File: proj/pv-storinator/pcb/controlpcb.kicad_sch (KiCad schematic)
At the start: 65 parts, among them J1 Conn_01x06_Socket, J10 Conn_01x01, J11 Conn_01x01, J12 Conn_01x06_Socket, J13 Conn_01x07_Socket, J14 Conn_01x01, J15 Conn_01x01, J16 Conn_01x04_Socket, J17 Conn_01x06_Socket, J18 Conn_01x01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

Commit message: pv-storinator: Improve mounting holes and R5 + R6 values
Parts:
- added H10, H7, H8, H9: MountingHole, MountingHole:MountingHole_2.2mm_M2_DIN965, symbol Mechanical:MountingHole
- J2, J3: footprint Custom_Footprints:SolderWire_D1.3mm_OD2.6mm -> Connector_Wire:SolderWire-0.75sqmm_1x01_D1.25mm_OD2.3mm
- R5: value 100k -> 47k
- R6: value 68k -> 47k
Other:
- note added: "Cable fixation holes"
- note added: "F1 must be slow-acting to prevent blow up when C1 needs to be charged."
- note added: "Use a zip tie or an insulated wire to hold the cables in place."
- moved on the sheet: C5, F1, J14, J15, R4, R6

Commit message: pv-storinator: Minor schematic improvements
- More efficient voltage regulator (lower quiescent current)
- SMD alternatives (hand soldering)
- Pull-Down on charge DC/DC for safety
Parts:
- added Q4_2: BSS316N / PJA3432 / DMG3406L / ?, Package_TO_SOT_SMD:SOT-23, symbol Transistor_FET:Q_NMOS_GSD
- added R1: 22k, Resistor_SMD:R_0805_2012Metric, symbol Device:R
- added U1_2: AP7381-50SA-7, Package_TO_SOT_SMD:SOT-23, symbol Regulator_Linear:AP7381-50SA-7
- U1_1: renamed from U1; value L78L05_TO92 -> AP7381-50V-A
- renumbered Q4 to Q4_1
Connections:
- net +5V: now also U1_2.2 (VO)
- net DCDC_EN: now also R1.1
- net GND: now also Q4_2.2 (S), R1.2, U1_2.3 (GND)
- net V_BAT: now also U1_2.1 (VI)
- net at Q4_1.2 (B), R16.2: now also Q4_2.1 (G)
- net at J22.1 (Pin_1), Q4_1.1 (C): now also Q4_2.3 (D)
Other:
- note added: "Q4_2 fits on the TO-92 footprint when soldering manually"
- note added: "R1: Force low in case the MCU has a failure."
- note added: "U1_2 fits on the TO-92 footprint when soldering manually"
- title: controlpcb Controller -> controlpcb

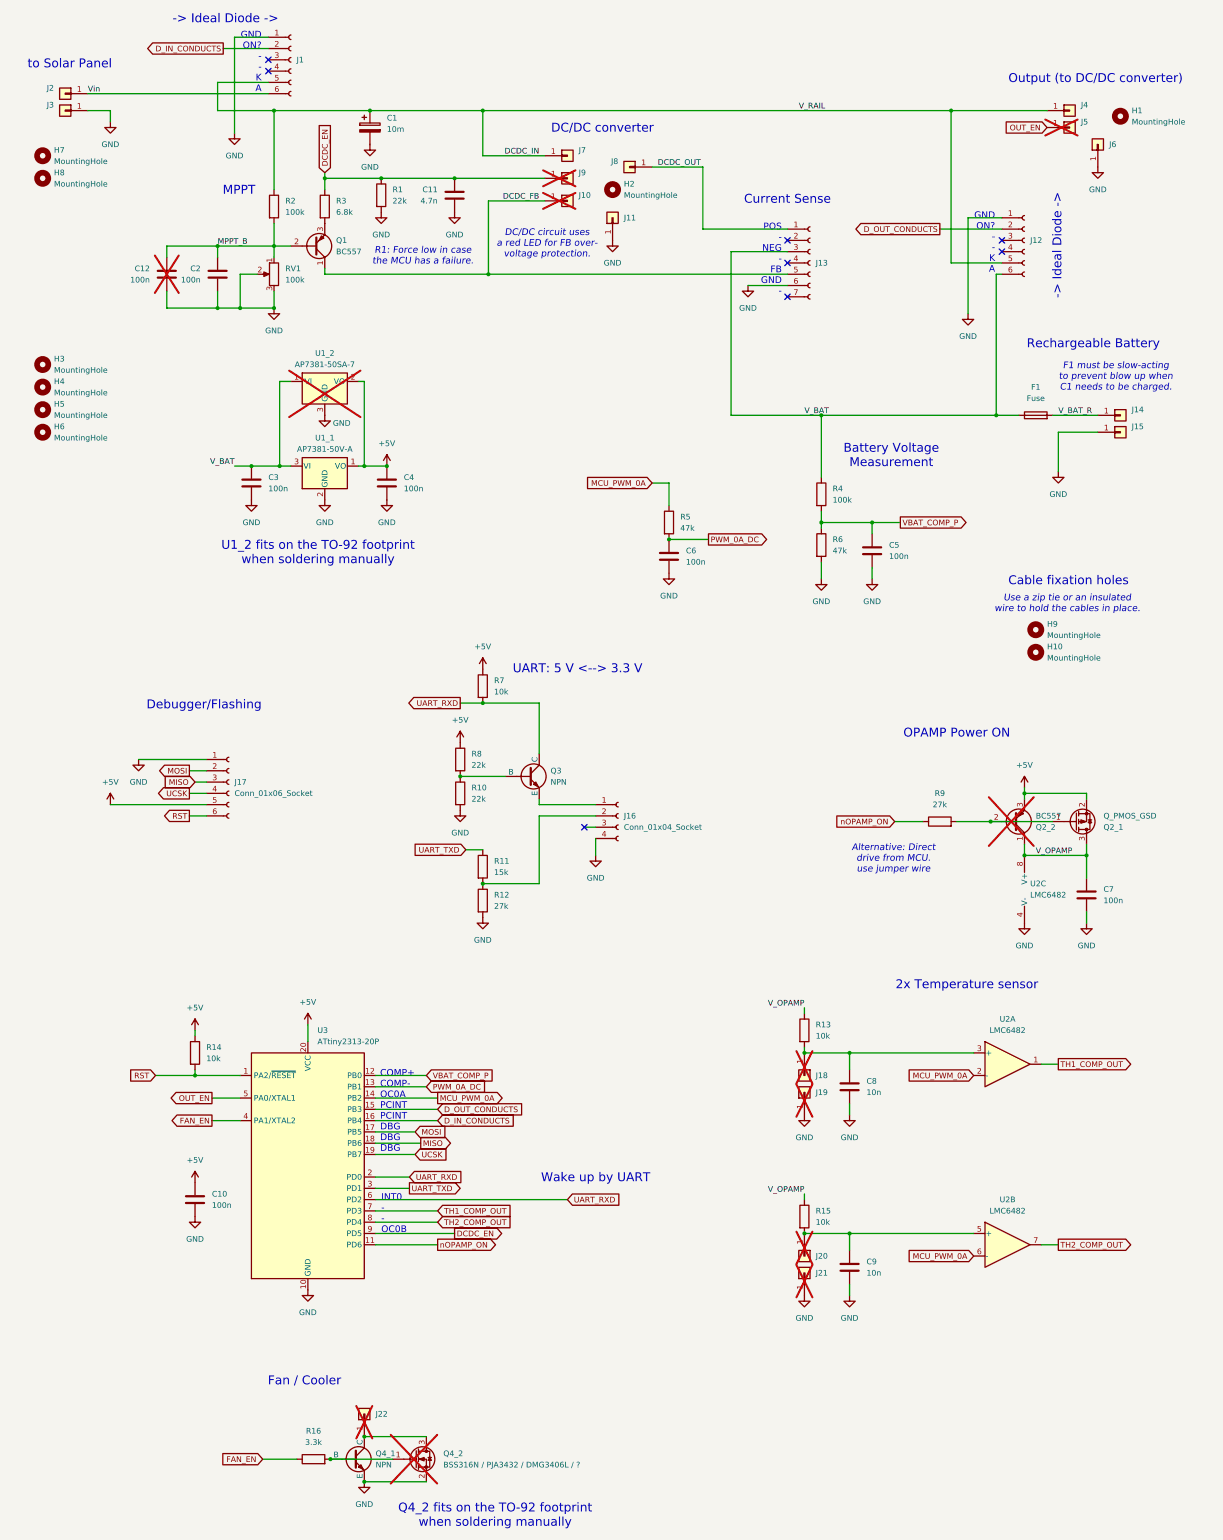
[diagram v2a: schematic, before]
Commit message: pv-storinator: Improve PCB
- Fix incorrect MCU_PWM_0A connection
- Add TVS (suppressor) diode for safety
- Enlarge holes for easier cable mounting
- Add custom footprint library (previously missing)
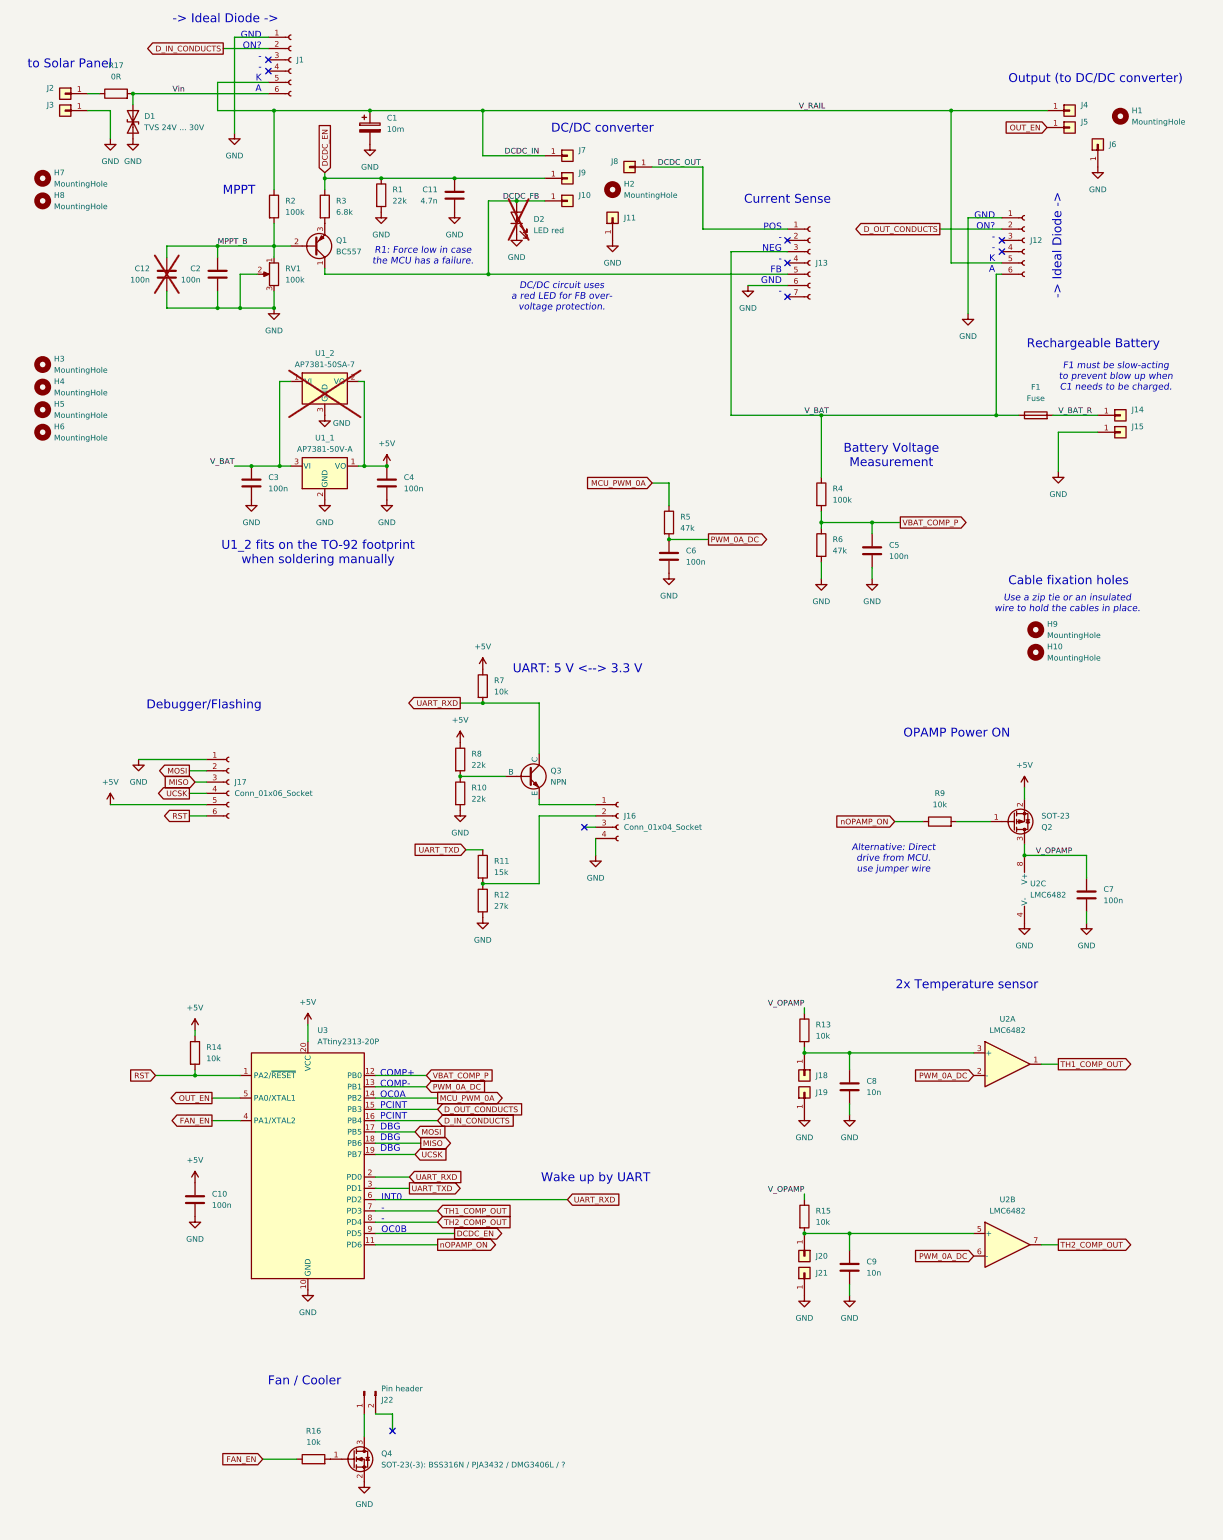
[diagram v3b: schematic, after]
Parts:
- removed J22: Conn_01x01, Connector_PinSocket_2.54mm:PinSocket_1x01_P2.54mm_Vertical, symbol Connector_Generic:Conn_01x01
- removed Q2_2: BC557, Custom_Footprints:TO-92_W, symbol Transistor_BJT:BC557
- removed Q4_1: NPN, Custom_Footprints:TO-92_W, symbol Simulation_SPICE:NPN
- added D1: TVS 24V ... 30V, Diode_SMD:D_SMA-SMB_Universal_Handsoldering, symbol Device:D_TVS
- added D2: LED red, LED_SMD:LED_0603_1608Metric, symbol Device:LED
- added J22: Pin header, Connector_PinHeader_2.54mm:PinHeader_1x02_P2.54mm_Vertical, symbol Connector:Conn_01x02_Pin
- added R17: 0R, Resistor_SMD:R_0805_2012Metric_Pad1.20x1.40mm_HandSolder, symbol Device:R
- H10, H7, H8, H9: footprint MountingHole:MountingHole_2.2mm_M2_DIN965 -> MountingHole:MountingHole_2.5mm
- J1, J12: footprint Custom_Symbols:SIP-6_Upright_Board -> Custom_Footprints:SIP-6_Upright_Board
- J10, J9: footprint Connector_PinSocket_2.54mm:PinSocket_1x01_P2.54mm_Vertical -> Connector_Wire:SolderWire-0.5sqmm_1x01_D0.9mm_OD2.1mm; now fitted
- J13: footprint Custom_Symbols:SIP-7_Upright_Board -> Custom_Footprints:SIP-7_Upright_Board
- J18, J19, J20, J21: footprint Connector_PinSocket_2.54mm:PinSocket_1x01_P2.54mm_Vertical -> Connector_PinHeader_2.54mm:PinHeader_1x01_P2.54mm_Vertical; now fitted; now in the parts list
- J5: footprint Connector_PinSocket_2.54mm:PinSocket_1x01_P2.54mm_Vertical -> Connector_Wire:SolderWire-0.5sqmm_1x01_D0.9mm_OD2.1mm; now fitted; now in the parts list
- Q2: renamed from Q2_1; value Q_PMOS_GSD -> SOT-23
- Q4: renamed from Q4_2; value BSS316N / PJA3432 / DMG3406L / ? -> SOT-23(-3): BSS316N / PJA3432 / DMG3406L / ?; footprint Package_TO_SOT_SMD:SOT-23 -> Package_TO_SOT_SMD:SOT-23-3; now fitted; now in the parts list
- R16: value 3.3k -> 10k; footprint Resistor_THT:R_Axial_DIN0207_L6.3mm_D2.5mm_P2.54mm_Vertical -> Resistor_SMD:R_0805_2012Metric_Pad1.20x1.40mm_HandSolder
- R9: value 27k -> 10k
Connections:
- net DCDC_FB: now also D2.2 (A)
- net GND: now also D1.2 (A2), D2.1 (K)
- net MCU_PWM_0A: no longer U2.2 (-), U2.6 (-)
- net PWM_0A_DC: now also U2.2 (-), U2.6 (-)
- net Vin: now also D1.1 (A1), R17.2; no longer J2.1 (Pin_1)
- net at Q4.3 (D): now also J22.1 (Pin_1)
- new net: J2.1 (Pin_1), R17.1
- no-connect marks 8 -> 9
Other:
- note removed: "Q4_2 fits on the TO-92 footprint when soldering manually"
- moved on the sheet: H7, H8, Q2
